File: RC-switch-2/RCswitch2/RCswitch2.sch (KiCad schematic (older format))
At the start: 10 parts, among them J1 Conn_01x03, J2 Conn_01x02, J3 Conn_01x02, J4 Conn_01x02, U1 4013, U2 PVG612

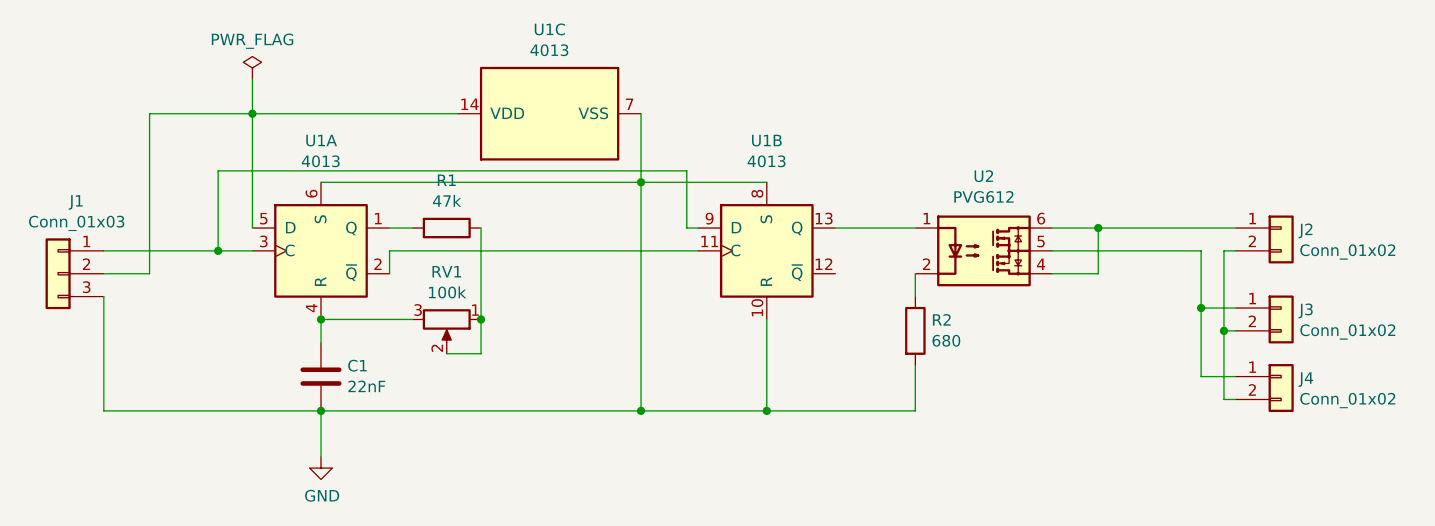
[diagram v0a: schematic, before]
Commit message: Done with RCswitch2. Production is ordered from JLCPCB
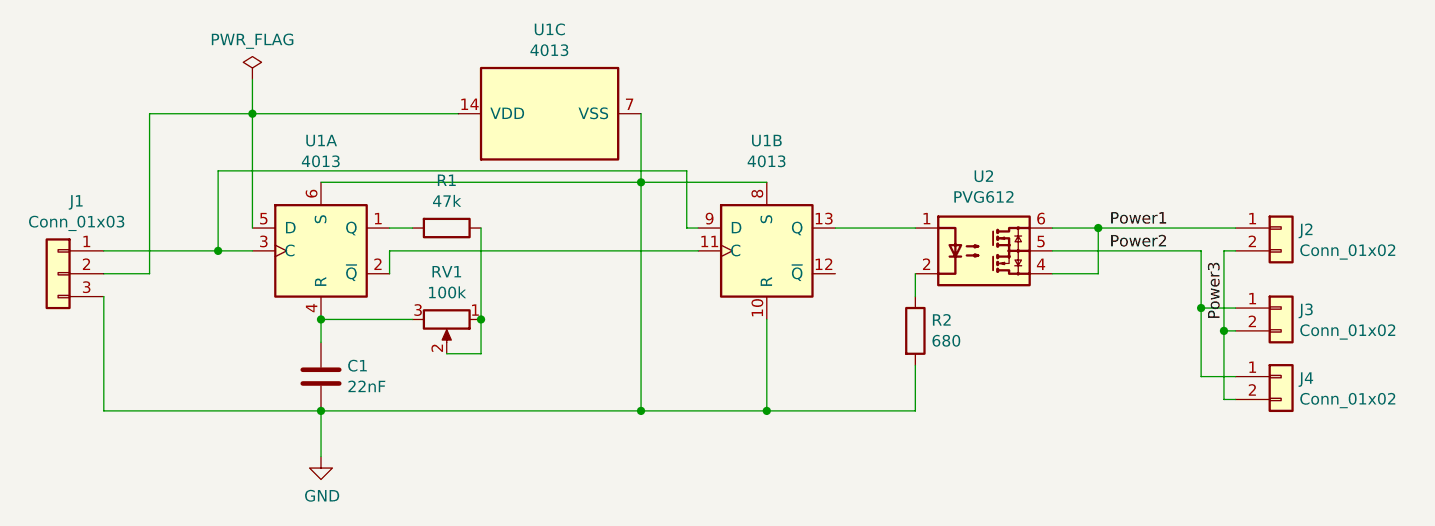
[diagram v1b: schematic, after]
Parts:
- J1: footprint Connector_PinSocket_2.54mm:PinSocket_1x03_P2.54mm_Vertical -> Connector_PinHeader_2.54mm:PinHeader_1x03_P2.54mm_Vertical
- J2, J3, J4: footprint Connector_PinSocket_2.54mm:PinSocket_1x02_P2.54mm_Vertical -> Connector_Molex:Molex_KK-254_AE-6410-02A_1x02_P2.54mm_Vertical
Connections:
- net Power1: now reaches J2.1 (Pin_1), U2.4, U2.6
- net Power2: now reaches J3.1 (Pin_1), J4.1 (Pin_1), U2.5
- net Power3: now reaches J2.2 (Pin_2), J3.2 (Pin_2), J4.2 (Pin_2)
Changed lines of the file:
@@
 F 0 "J1" H 1418 2867 50  0000 C CNN
 F 1 "Conn_01x03" H 1418 2776 50  0000 C CNN
-F 2 "Connector_PinSocket_2.54mm:PinSocket_1x03_P2.54mm_Vertical" H 1500 2550 50  0001 C CNN
+F 2 "Connector_PinHeader_2.54mm:PinHeader_1x03_P2.54mm_Vertical" H 1500 2550 50  0001 C CNN
 F 3 "~" H 1500 2550 50  0001 C CNN
 	1    1500 2550
@@
 F 0 "J2" H 6930 2342 50  0000 L CNN
 F 1 "Conn_01x02" H 6930 2251 50  0000 L CNN
-F 2 "Connector_PinSocket_2.54mm:PinSocket_1x02_P2.54mm_Vertical" H 6850 2350 50  0001 C CNN
+F 2 "Connector_Molex:Molex_KK-254_AE-6410-02A_1x02_P2.54mm_Vertical" H 6850 2350 50  0001 C CNN
 F 3 "~" H 6850 2350 50  0001 C CNN
 	1    6850 2350
@@
 F 0 "J3" H 6930 2692 50  0000 L CNN
 F 1 "Conn_01x02" H 6930 2601 50  0000 L CNN
-F 2 "Connector_PinSocket_2.54mm:PinSocket_1x02_P2.54mm_Vertical" H 6850 2700 50  0001 C CNN
+F 2 "Connector_Molex:Molex_KK-254_AE-6410-02A_1x02_P2.54mm_Vertical" H 6850 2700 50  0001 C CNN
 F 3 "~" H 6850 2700 50  0001 C CNN
 	1    6850 2700
@@
 F 0 "J4" H 6930 2992 50  0000 L CNN
 F 1 "Conn_01x02" H 6930 2901 50  0000 L CNN
-F 2 "Connector_PinSocket_2.54mm:PinSocket_1x02_P2.54mm_Vertical" H 6850 3000 50  0001 C CNN
+F 2 "Connector_Molex:Molex_KK-254_AE-6410-02A_1x02_P2.54mm_Vertical" H 6850 3000 50  0001 C CNN
 F 3 "~" H 6850 3000 50  0001 C CNN
 	1    6850 3000
@@
 Wire Wire Line
 	5250 2950 5250 3150
+Text Label 6100 2350 0    50   ~ 0
+Power1
+Text Label 6100 2450 0    50   ~ 0
+Power2
+Text Label 6600 2750 1    50   ~ 0
+Power3
 $EndSCHEMATC
